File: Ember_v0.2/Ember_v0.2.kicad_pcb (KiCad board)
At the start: 2 copper layers, 87 parts, among them J3 DROGUE, J4 BATT_CONN, J5 MAIN, J6 MAN2, J7 DROGUE2, J8 ARM, Q1 SISA96DN-T1, Q2 SISA96DN-T1, Q3 SISA96DN-T1, Q4 SISA96DN-T1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

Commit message: board route almost complete
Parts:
- added JP6: ~, microbuilder:1X02_OVAL, F.Cu at (97.5, 137.8)
- added Q6: SISA96DN-T1, SISA96DN-T1-GE3:SIS862DNT1GE3, F.Cu at (97.3, 131.5)
- added R23: 33k, microbuilder:0603, F.Cu at (101.8, 131.2)
- added R24: 1k, microbuilder:0603, F.Cu at (99.7, 127.7)
- added REF**: MountingHole_3mm, MountingHole:MountingHole_3mm, F.Cu at (114.9, 99.7)
- added REF**: MountingHole_3mm, MountingHole:MountingHole_3mm, F.Cu at (85.6, 53.0)
- added REF**: MountingHole_3mm, MountingHole:MountingHole_3mm, F.Cu at (147.5, 53.0)
- added REF**: MountingHole_3mm, MountingHole:MountingHole_3mm, F.Cu at (149.9, 119.7)
- added REF**: MountingHole_3mm, MountingHole:MountingHole_3mm, F.Cu at (85.6, 139.5)
- added REF**: MountingHole_3mm, MountingHole:MountingHole_3mm, F.Cu at (149.9, 99.7)
- added REF**: MountingHole_3mm, MountingHole:MountingHole_3mm, F.Cu at (147.6, 139.5)
- C3, C4, C8, C9, JP2, JP3, JP4, JP5, R10, R11, R12, R16, R18, R25, R26, R34, R35, R36, R37, R9, U6, U8: moved to B.Cu
- moved R37 92.5 mm to (121.2, 133.6), turned to -90 degrees
- moved C1 92.0 mm to (134.8, 79.8), turned to 180 degrees
- moved IC1 88.7 mm to (145.8, 68.6), turned to -90 degrees
- moved R10 86.9 mm to (102.0, 131.5), turned to -90 degrees
- moved R9 86.7 mm to (104.5, 128.6), turned to -90 degrees
- moved R11 86.2 mm to (104.5, 133.3), turned to -90 degrees
- moved U5 81.4 mm to (142.2, 82.6), turned to 180 degrees
- moved R12 79.6 mm to (110.1, 128.7), turned to -90 degrees
- moved R16 76.9 mm to (107.6, 131.5), turned to -90 degrees
- moved R34 74.3 mm to (115.7, 133.4), turned to -90 degrees
- moved R18 74.0 mm to (110.1, 133.4), turned to -90 degrees
- moved LED3 73.5 mm to (149.2, 125.3)
- moved R43 73.5 mm to (149.3, 132.4)
- moved R44 73.5 mm to (149.3, 127.7)
- moved LED2 73.5 mm to (149.2, 130.1)
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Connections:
- U7 pad P$5: unconnected-(U7-GP3-PadP$5) -> /CAM
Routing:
- net /3v3: track 19.4 -> 287.4 mm, vias 0 -> 10
- net Net-(U5-AIN3): track 0.00 -> 108.7 mm, vias 0 -> 1
- net /V_BATT: track 62.2 -> 150.1 mm
- net Net-(U5-AIN2): track 2.60 -> 78.2 mm, vias 0 -> 1
- net /ADS_DRDY_1: track 0.00 -> 71.3 mm, vias 0 -> 1
- net /ADS_MISO: track 0.00 -> 70.5 mm, vias 0 -> 1
- net /ADS_CS_1: track 0.00 -> 69.4 mm, vias 0 -> 3
- net /B2B_TX: track 0.25 -> 69.1 mm
- net /B2B_RX: track 0.01 -> 68.7 mm
- net /ADS_MOSI: track 0.00 -> 66.4 mm, vias 0 -> 1
- net /ADS_SCLK: track 0.00 -> 63.4 mm, vias 0 -> 3
- net /ADS_DRDY_2: track 0.00 -> 62.4 mm, vias 0 -> 1
- net /SCL: track 43.8 -> 104.8 mm
- net /CAM: track 0.00 -> 56.0 mm
- net /SDA: track 53.5 -> 108.3 mm
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- added copper zone on F.Cu, net /3v3
- added copper zone on B.Cu, net /GND
- added copper zone on F.Cu, net /GND
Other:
- board outline added: 75 x 99.5 mm

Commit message: did some graphic things on silkscreen
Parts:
- added ?: , drogue_label:DROGUE0, F.Cu at (81.2, 105.8)
- added ?: , gnd_label:GND0, F.Cu at (131.6, 56.6)
- added ?: , main_label:MAIN0, F.Cu at (81.1, 116.7)
- added ?: , 7v4_label:7V40, F.Cu at (128.9, 56.6)
- added ?: , main_label:MAIN0, F.Cu at (81.2, 92.3)
- added ?: , drogue_label:DROGUE0, F.Cu at (81.0, 130.6)
- added ?: , tx_label:TX0, F.Cu at (136.7, 56.6)
- added ?: , rx_label:RX0, F.Cu at (134.1, 56.6)
- added G***: LOGO, RT_Graphics:Ember_logo, F.Cu at (137.2, 71.1)
- added G***: LOGO, RT_Graphics:FCU_label, F.Cu at (146.9, 59.5)
- added G***: LOGO, RT_Graphics:RT_logo, F.Cu at (97.8, 51.5)
- added G***: LOGO, RT_Graphics:ARM_label, F.Cu at (81.3, 77.2)
- added G***: LOGO, RT_Graphics:RT_logo_hi_res, B.Cu at (127.2, 94.6)
- added REF**: KiCad-Logo2_5mm_SilkScreen, Symbol:KiCad-Logo2_5mm_SilkScreen, F.Cu at (119.8, 51.4)
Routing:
- net /V_BATT: track 150.1 -> 152.7 mm
- net /CAM: track 56.0 -> 58.4 mm
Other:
- outline, holes or cut-outs redrawn
- board text added: "EMBER V0.2"
- board text added: "March 2026"

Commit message: Added some assets and V0.2 is sent for review
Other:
- board text added: "{dblquote}To the team for the chaos the late nights and everything we learned on March 15{dblquote}"

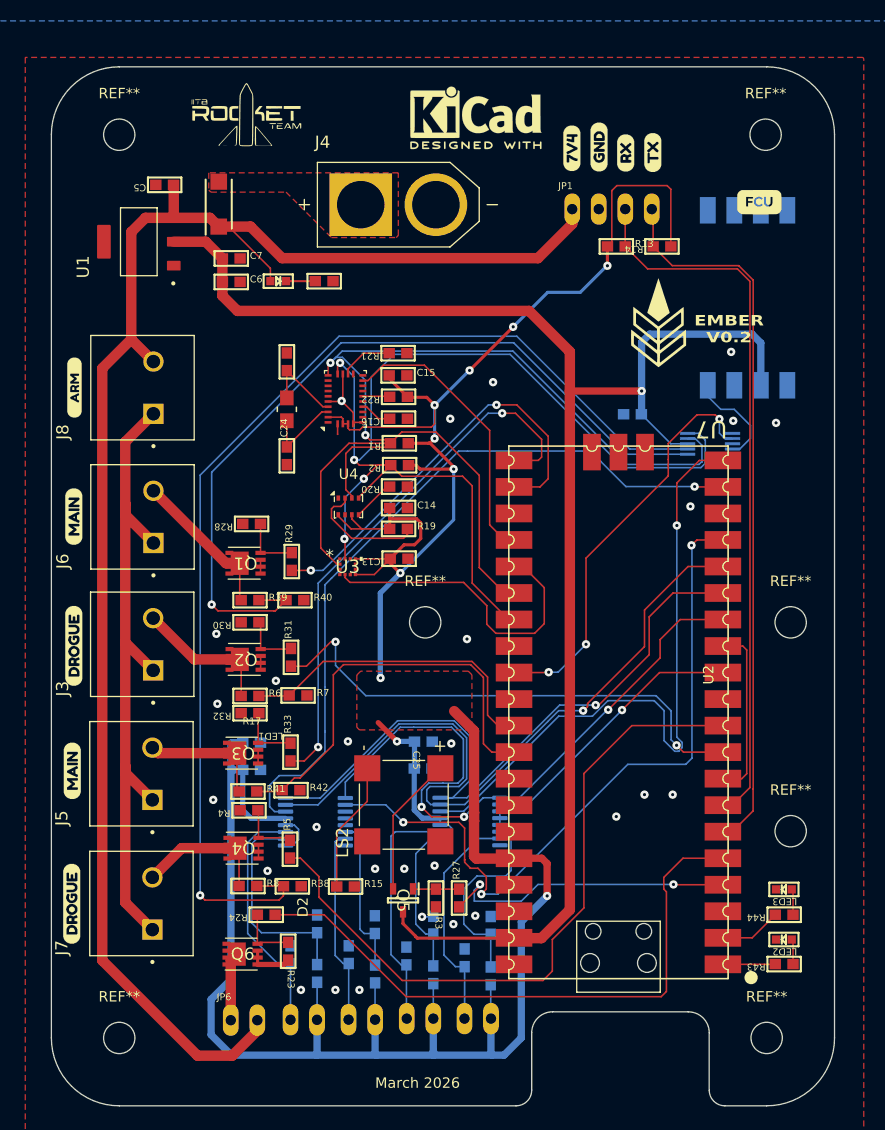
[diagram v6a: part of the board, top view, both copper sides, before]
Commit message: All relevant DRC errors are resolved
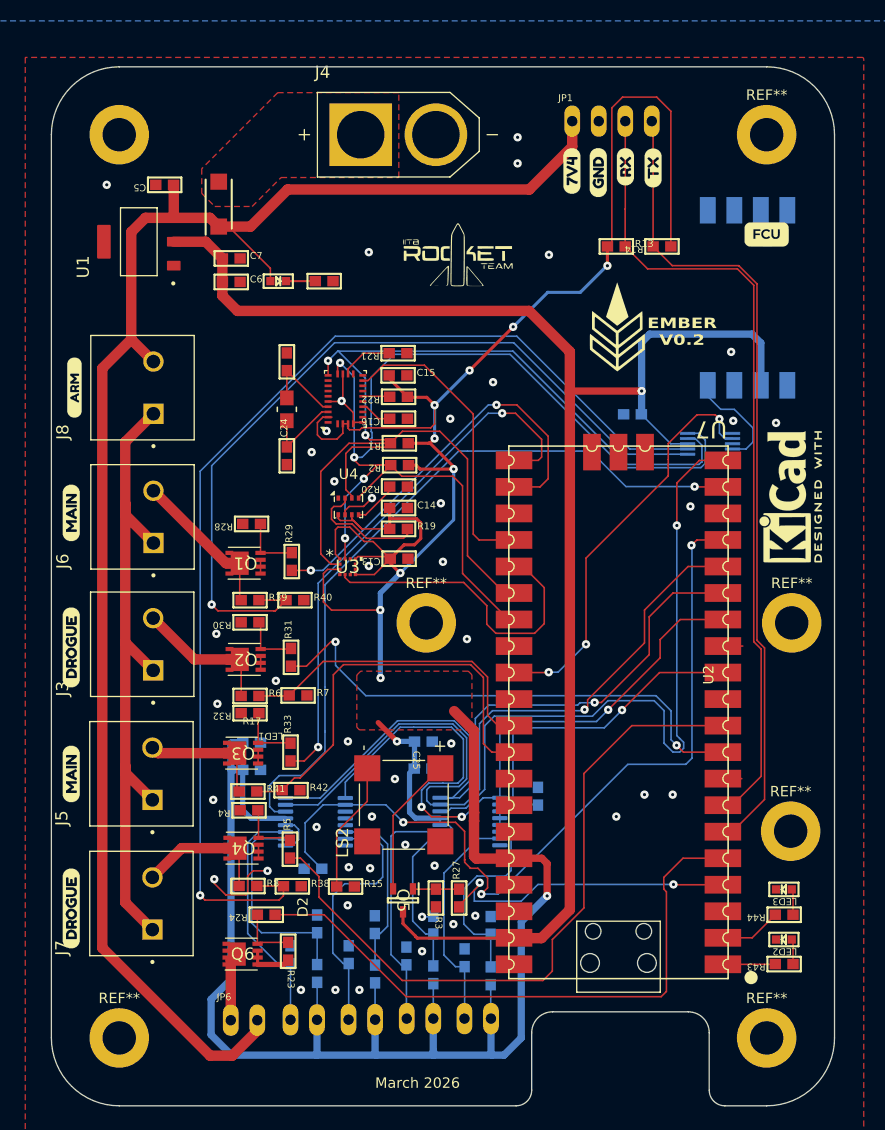
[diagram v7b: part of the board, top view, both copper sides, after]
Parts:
- removed the ? at (81.2, 105.8)
- removed the ? at (81.1, 116.7)
- removed the ? at (81.2, 92.3)
- removed the ? at (81.0, 130.6)
- removed the REF** at (114.9, 99.7)
- removed the REF** at (85.6, 53.0)
- removed the REF** at (147.5, 53.0)
- removed the REF** at (149.9, 119.7)
- removed the REF** at (85.6, 139.5)
- removed the REF** at (149.9, 99.7)
- removed the REF** at (147.6, 139.5)
- added ?: , drogue_label:DROGUE0, F.Cu at (81.0, 106.0)
- added ?: , drogue_label:DROGUE0, F.Cu at (81.0, 131.0)
- added ?: , main_label:MAIN0, F.Cu at (81.0, 92.0)
- added ?: , main_label:MAIN0, F.Cu at (81.0, 117.0)
- added R45: 10k, microbuilder:0603, B.Cu at (104.2, 123.3)
- added R46: 10k, microbuilder:0603, B.Cu at (125.7, 116.3)
- added REF**: MountingHole_3.2mm_M3_ISO7380_Pad, MountingHole:MountingHole_3.2mm_M3_ISO7380_Pad, F.Cu at (150.0, 99.8)
- added REF**: MountingHole_3.2mm_M3_ISO7380_Pad, MountingHole:MountingHole_3.2mm_M3_ISO7380_Pad, F.Cu at (85.6, 53.0)
- added REF**: MountingHole_3.2mm_M3_ISO7380_Pad, MountingHole:MountingHole_3.2mm_M3_ISO7380_Pad, F.Cu at (147.6, 139.5)
- added REF**: MountingHole_3.2mm_M3_ISO7380_Pad, MountingHole:MountingHole_3.2mm_M3_ISO7380_Pad, F.Cu at (149.9, 119.7)
- added REF**: MountingHole_3.2mm_M3_ISO7380_Pad, MountingHole:MountingHole_3.2mm_M3_ISO7380_Pad, F.Cu at (85.6, 139.5)
- added REF**: MountingHole_3.2mm_M3_ISO7380_Pad, MountingHole:MountingHole_3.2mm_M3_ISO7380_Pad, F.Cu at (115.0, 99.8)
- added REF**: MountingHole_3.2mm_M3_ISO7380_Pad, MountingHole:MountingHole_3.2mm_M3_ISO7380_Pad, F.Cu at (147.6, 53.0)
- moved REF** 47.2 mm to (149.9, 87.7), turned to 90 degrees
- moved G*** 24.3 mm to (118.0, 64.9)
- moved JP1 8.42 mm to (132.8, 51.7)
- moved J4 6.70 mm to (112.3, 53.0)
- moved G*** 3.97 mm to (133.2, 71.5)
- moved G*** 3.18 mm to (147.6, 62.6)
- moved ? 2.45 mm to (131.5, 59.0)
- moved ? 2.17 mm to (128.9, 58.8)
- moved ? 1.48 mm to (136.7, 58.1)
- moved ? 1.33 mm to (134.1, 58.0)
- moved G*** 1.05 mm to (127.3, 93.6)
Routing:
- net /3v3: track 287.4 -> 328.9 mm, vias 10 -> 11
- net /ADS_CS_1: track 69.4 -> 79.0 mm
- net /B2B_TX: track 69.1 -> 78.4 mm
- net /B2B_RX: track 68.7 -> 78.0 mm
- net /ADS_CS_2: track 26.6 -> 34.1 mm
- net /ACT2: track 19.0 -> 25.2 mm
- net /ADS_DRDY_2: track 62.4 -> 66.3 mm
- net /ADS_SCLK: track 63.4 -> 67.1 mm
- net /ADS_MISO: track 70.5 -> 74.2 mm
- net /ADS_MOSI: track 66.4 -> 70.0 mm
- net /GND: track 37.4 -> 34.9 mm, vias 28 -> 46
- net /REF2: track 15.0 -> 17.0 mm
- net /BNO_INT: track 27.3 -> 28.8 mm
- net /V_BATT: track 152.7 -> 153.6 mm
- net /SCL: track 104.8 -> 104.1 mm
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
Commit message: All routings completed, Lisan Al-gaib!
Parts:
- moved REF** 3.10 mm to (111.9, 99.7)
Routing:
- net /DROGUE: track 49.7 -> 47.9 mm
- net /3v3: track 328.9 -> 329.8 mm
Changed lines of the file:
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@@
 	(footprint "MountingHole:MountingHole_3.2mm_M3_ISO7380_Pad"
 		(layer "F.Cu")
-		(at 115 99.75)
+		(at 111.9 99.7)
 		(descr "Mounting Hole 3.2mm, M3, generated by kicad-footprint-generator mountinghole.py")
 		(tags "mountinghole M3 ISO7380")
@@
 		(layer "F.SilkS")
 		(pts
-			(xy 114.9 99.7) (xy 149.9 99.7)
+			(xy 111.9 99.7) (xy 149.9 99.7)
 		)
 		(height 0)
@@
 			(keep_text_aligned yes)
 		)
-		(gr_text "35"
-			(at 132.4 98.6 0)
+		(gr_text "38"
+			(at 130.9 98.6 0)
 			(layer "F.SilkS")
 			(effects
@@
 	)
 	(segment
+		(start 106.975 98.425)
+		(end 106.875 98.525)
+		(width 0.154)
+		(layer "F.Cu")
+		(net 3)
+	)
+	(segment
+		(start 105.925 98.525)
+		(end 105.15 97.75)
+		(width 0.154)
+		(layer "F.Cu")
+		(net 3)
+	)
+	(segment
 		(start 106.3 90.825)
 		(end 106.3 93.175)
@@
 	)
 	(segment
+		(start 105.15 97.75)
+		(end 105.15 95.025)
+		(width 0.154)
+		(layer "F.Cu")
+		(net 3)
+	)
+	(segment
 		(start 107.875 89.804)
 		(end 108.821 90.75)
@@
 	)
 	(segment
-		(start 105.15 95.025)
-		(end 105.55 94.625)
-		(width 0.154)
-		(layer "F.Cu")
-		(net 3)
-	)
-	(segment
 		(start 115.35 82.55)
 		(end 115.8 82.1)
@@
 	)
 	(segment
-		(start 105.925 98.525)
-		(end 105.15 97.75)
+		(start 106.875 98.525)
+		(end 105.925 98.525)
 		(width 0.154)
 		(layer "F.Cu")
@@
 	)
 	(segment
-		(start 105.55 94.625)
-		(end 106.7257 94.625)
-		(width 0.154)
-		(layer "F.Cu")
-		(net 3)
-	)
-	(segment
 		(start 119.575 117.924426)
 		(end 119.58 117.929426)
@@
 	)
 	(segment
-		(start 110.6 98.525)
-		(end 105.925 98.525)
-		(width 0.154)
-		(layer "F.Cu")
-		(net 3)
-	)
-	(segment
 		(start 106.3 93.175)
 		(end 106.7257 93.6007)
@@
 	)
 	(segment
-		(start 105.15 97.75)
-		(end 105.15 95.025)
-		(width 0.154)
-		(layer "F.Cu")
-		(net 3)
-	)
-	(segment
 		(start 110.4 109.3)
 		(end 112.2 111.1)
@@
 	)
 	(segment
+		(start 105.55 94.625)
+		(end 106.7257 94.625)
+		(width 0.154)
+		(layer "F.Cu")
+		(net 3)
+	)
+	(segment
 		(start 111.5 88.75)
 		(end 111.5 89.75)
@@
 	)
 	(segment
+		(start 105.15 95.025)
+		(end 105.55 94.625)
+		(width 0.154)
+		(layer "F.Cu")
+		(net 3)
+	)
+	(segment
 		(start 117.625 84.8)
 		(end 115.375 82.55)
@@
 	)
 	(via
-		(at 110.6 98.525)
+		(at 106.975 98.425)
 		(size 0.8)
 		(drill 0.3)
@@
 	)
 	(segment
+		(start 106.975 98.425)
+		(end 106.975 101.8)
+		(width 0.5)
+		(layer "B.Cu")
+		(net 3)
+	)
+	(segment
 		(start 122.45 141.15)
 		(end 121.3 141.15)
@@
 	)
 	(segment
-		(start 110.6 96.9)
-		(end 112.525 94.975)
-		(width 0.5)
-		(layer "B.Cu")
-		(net 3)
-	)
-	(segment
 		(start 126.625 68.1)
 		(end 129.75 68.1)
@@
 	)
 	(segment
+		(start 110.6 105)
+		(end 110.625 105.025)
+		(width 0.5)
+		(layer "B.Cu")
+		(net 3)
+	)
+	(segment
 		(start 110.2 141.15)
 		(end 110.1 141.05)
@@
 	)
 	(segment
+		(start 110.175 105)
+		(end 110.6 105)
+		(width 0.5)
+		(layer "B.Cu")
+		(net 3)
+	)
+	(segment
 		(start 121.175 134.4)
 		(end 121.175 137.625)
@@
 	)
 	(segment
+		(start 106.975 101.8)
+		(end 110.175 105)
+		(width 0.5)
+		(layer "B.Cu")
+		(net 3)
+	)
+	(segment
 		(start 115.7 141.15)
 		(end 110.2 141.15)
@@
 	)
 	(segment
-		(start 110.625 105.025)
-		(end 110.6 105)
-		(width 0.5)
-		(layer "B.Cu")
-		(net 3)
-	)
-	(segment
 		(start 113.8532 111.1)
 		(end 113.875 111.1218)
@@
 	)
 	(segment
-		(start 110.6 98.525)
-		(end 110.6 96.9)
+		(start 106.975 98.425)
+		(end 110.4 95)
 		(width 0.5)
 		(layer "B.Cu")
@@
 	)
 	(segment
-		(start 110.6 105)
-		(end 110.6 98.525)
-		(width 0.5)
+		(start 102.2 121.075)
+		(end 101.525 121.075)
+		(width 0.154)
 		(layer "B.Cu")
 		(net 3)
 	)
 	(segment
-		(start 102.2 121.075)
-		(end 101.525 121.075)
-		(width 0.154)
+		(start 110.4 95)
+		(end 112.5 95)
+		(width 0.5)
 		(layer "B.Cu")
 		(net 3)
@@
 	)
 	(segment
+		(start 112.5 95)
+		(end 112.525 94.975)
+		(width 0.5)
+		(layer "B.Cu")
+		(net 3)
+	)
+	(segment
 		(start 96.3282 113.8282)
 		(end 97.425 113.8282)
@@
 	)
 	(segment
-		(start 103.525 103.9)
-		(end 102.05 103.9)
+		(start 106.312026 102.8)
+		(end 104.625 102.8)
 		(width 0.154)
 		(layer "F.Cu")
@@
 	)
 	(segment
-		(start 139.63 112.13)
-		(end 143.41 112.13)
+		(start 103.525 103.9)
+		(end 102.05 103.9)
 		(width 0.154)
 		(layer "F.Cu")
@@
 	)
 	(segment
-		(start 105.862974 101.562026)
-		(end 103.525 103.9)
+		(start 139.63 112.13)
+		(end 143.41 112.13)
 		(width 0.154)
 		(layer "F.Cu")
@@
 	)
 	(segment
-		(start 106.312026 101.562026)
-		(end 105.862974 101.562026)
+		(start 104.625 102.8)
+		(end 103.525 103.9)
 		(width 0.154)
 		(layer "F.Cu")
@@
 	)
 	(via
-		(at 106.312026 101.562026)
+		(at 106.312026 102.8)
 		(size 0.8)
 		(drill 0.3)
@@
 	)
 	(segment
-		(start 106.312026 103.82408)
-		(end 109.212946 106.725)
+		(start 109.212946 106.725)
+		(end 137 106.725)
 		(width 0.154)
 		(layer "B.Cu")
@@
 	)
 	(segment
-		(start 109.212946 106.725)
-		(end 137 106.725)
+		(start 138.45 110.95)
+		(end 138.975 111.475)
 		(width 0.154)
 		(layer "B.Cu")
@@
 	)
 	(segment
-		(start 106.312026 101.562026)
+		(start 106.312026 102.8)
 		(end 106.312026 103.82408)
 		(width 0.154)
@@
 	)
 	(segment
-		(start 138.45 110.95)
-		(end 138.975 111.475)
+		(start 138.45 108.175)
+		(end 138.45 110.95)
 		(width 0.154)
 		(layer "B.Cu")
@@
 	)
 	(segment
-		(start 138.45 108.175)
-		(end 138.45 110.95)
+		(start 106.312026 103.82408)
+		(end 109.212946 106.725)
 		(width 0.154)
 		(layer "B.Cu")
